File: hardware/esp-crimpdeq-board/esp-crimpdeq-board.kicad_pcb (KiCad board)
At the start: 2 copper layers, 22.9 x 63.5 mm, 95 parts, among them J1 USB4105-GF-A, Q1 DMG3415U, SW1 SW_Push, SW2 SW_Push, U1 SHTC3, U2 ICM-42670-P, U3 ESP32-C3-MINI-1, U4 Rust_Board, U5 SY8088, U6 MCP73831T-2ACI/OT, Y1 32.768Hz

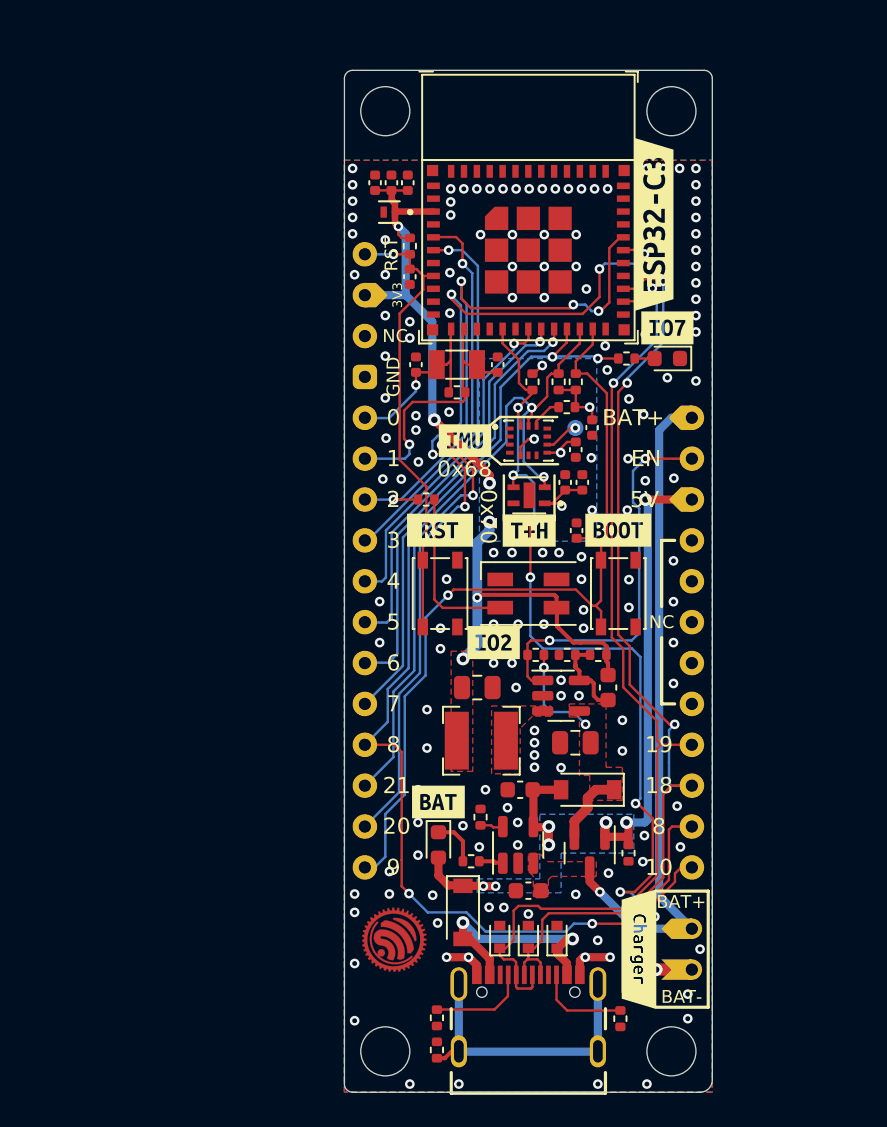
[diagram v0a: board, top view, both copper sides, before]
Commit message: Updated espressif kicad libraries and removed some unecessary libs
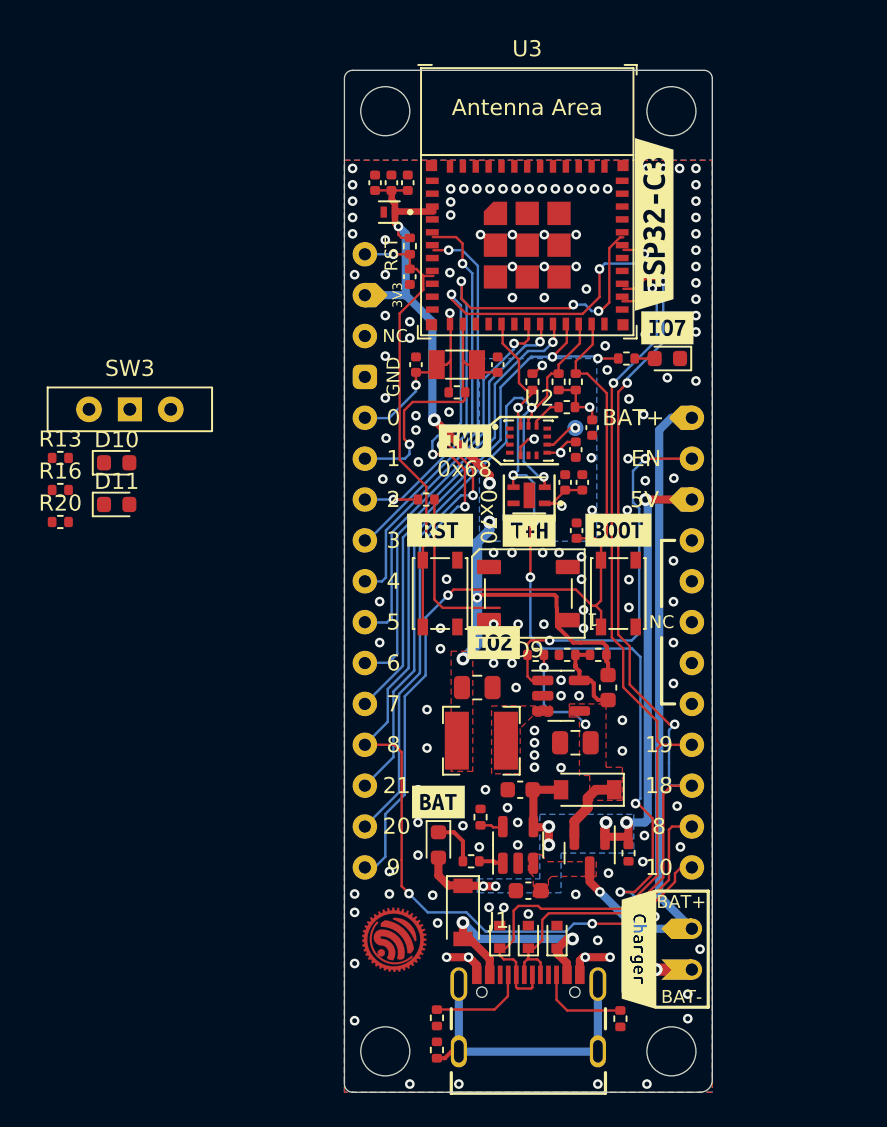
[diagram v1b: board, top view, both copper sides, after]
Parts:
- added D10: LED, LED_SMD:LED_0603_1608Metric, F.Cu at (122.5, 89.4)
- added D11: LED, LED_SMD:LED_0603_1608Metric, F.Cu at (122.5, 92.0)
- added R13: 470R 1%, Resistor_SMD:R_0402_1005Metric, F.Cu at (119.0, 89.1)
- added R16: 470R 1%, Resistor_SMD:R_0402_1005Metric, F.Cu at (119.0, 91.1)
- added R20: 10kR 1%, Resistor_SMD:R_0402_1005Metric, F.Cu at (119.0, 93.1)
- added SW3: SW_Wuerth_450301014042, Button_Switch_THT:SW_Slide-03_Wuerth-WS-SLTV_10x2.5x6.4_P2.54mm, F.Cu at (123.3, 86.1)
- D9: footprint LED_SMD:LED_SK6812MINI_PLCC4_3.5x3.5mm_P1.75mm -> LED_SMD:LED_WS2812B_PLCC4_5.0x5.0mm_P3.2mm
- U3: footprint Espressif:ESP32-C3-MINI-1 -> PCM_Espressif:ESP32-C3-MINI-1
- moved U3 3.01 mm to (148.0, 73.2)
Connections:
- R1 pad 2: ENABLE -> Net-(SW3-A)

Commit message: Changed link libraries
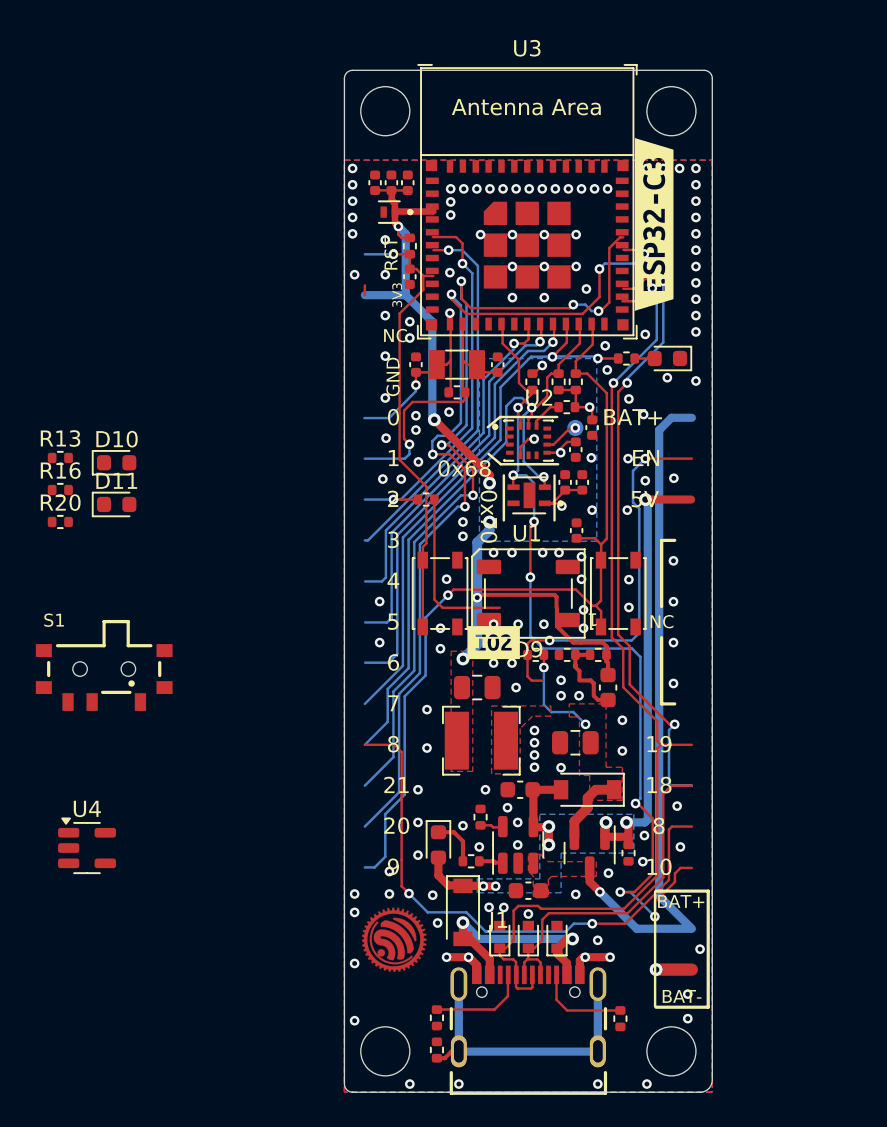
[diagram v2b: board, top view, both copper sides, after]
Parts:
- removed REF**: logo_HF, Rust_Board:logo_HF
- removed REF**: logo_HF, Rust_Board:logo_PB
- removed SW3: SW_Wuerth_450301014042, Button_Switch_THT:SW_Slide-03_Wuerth-WS-SLTV_10x2.5x6.4_P2.54mm
- removed U5: SY8088, Package_TO_SOT_SMD:SOT-23-5
- removed kibuzzard-61B9CCBB, kibuzzard-61B9CE3D, kibuzzard-61B9CE86, kibuzzard-61B9CEAB, kibuzzard-61B9EF98, kibuzzard-61C05335, kibuzzard-61C057D5, kibuzzard-61C057FD, kibuzzard-61C05804, kibuzzard-61C0588C, kibuzzard-61C05909, kibuzzard-61C05949, kibuzzard-61C05975, kibuzzard-61C0597E, kibuzzard-61C05A1A, kibuzzard-61C05A22, kibuzzard-61C05B60, kibuzzard-61C05BAC, kibuzzard-61C05C0D, kibuzzard-61C05C87, kibuzzard-61C05C92, kibuzzard-61C05D58, kibuzzard-61C05D75, kibuzzard-61C05DB0, kibuzzard-61C0F315, kibuzzard-61C0F325, kibuzzard-61C0F363, kibuzzard-61C0F3FF, kibuzzard-61C0F406, kibuzzard-61C0F511, kibuzzard-61C0F551: G***, label
- added S1: 450404015514, PCM_Wurth_Elektronik:450404015514, F.Cu at (121.7, 102.2)
- J1: footprint Rust_Board:GCT_USB4105-GF-A -> PCM_GCT:GCT_USB4105-GF-A
- U1: footprint Rust_Board:SON100P200X200X80-5N -> PCM_Sensirion:SON100P200X200X80-5N
- U2: footprint Rust_Board:IC_ICM-42670-P -> PCM_TDK_InvenSense:IC_ICM-42670-P
- U4: value Rust_Board -> SY8088; footprint Rust_Board:Rust_Board -> Package_TO_SOT_SMD:SOT-23-5
- moved U4 32.4 mm to (120.7, 113.3)
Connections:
- C6 pad 2: Net-(U5-FB) -> Net-(U4-FB)
- R2 pad 2: Net-(U5-FB) -> Net-(U4-FB)
- R3 pad 1: Net-(U5-FB) -> Net-(U4-FB)
- U4 pad 1: CHIP_PU -> ENABLE
- U4 pad 2: +3V3 -> GND
- U4 pad 3: unconnected-(U4-Pad3) -> /Buck_Coil
- U4 pad 4: GND -> +5V
- U4 pad 5: IO0 -> Net-(U4-FB)
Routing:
- net IO21_TX: track 52.2 -> 0.00 mm, vias 5 -> 0
- net IO20_RX: track 55.3 -> 107.5 mm, vias 5 -> 10
- net Net-(R1-Pad2): track 0.00 -> 24.5 mm, vias 0 -> 2
- net ENABLE: track 24.5 -> 0.00 mm, vias 2 -> 0
- net Net-(U5-FB): track 5.25 -> 0.00 mm
- net Net-(U4-FB): track 0.00 -> 5.25 mm

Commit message: Added notes
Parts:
- removed G***: LOGO, Rust_Board:esp-rs_logo_4mm
- removed kibuzzard-61E1AB2E: G***, kibuzzard-61E1AB2E
- removed kibuzzard-61F26841: G***, kibuzzard-61F26841
- removed kibuzzard-61F26855: G***, kibuzzard-61F26855
- removed kibuzzard-61F2685B: G***, kibuzzard-61F2685B
- removed kibuzzard-6269032F: G***, kibuzzard-6269032F
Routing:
- net VBUS: track 39.3 -> 36.5 mm
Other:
- outline, holes or cut-outs redrawn
- board text removed: "-"
- board text removed: "0"
- board text removed: "1"
- board text removed: "1.6mm"
- board text removed: "10"
- board text removed: "18"
- board text removed: "19"
- board text removed: "2"
- board text removed: "20"
- board text removed: "2022-04-27"
- board text removed: "21"
- board text removed: "3"
- board text removed: "4"
- board text removed: "5"
- board text removed: "5V"
- board text removed: "6"
- board text removed: "7"
- board text removed: "8"
- board text removed: "9"
- board text removed: "BAT+"
- board text removed: "BAT-"
- board text removed: "Base Copper (oz)"
- board text removed: "Copper 1 OZ"
- board text removed: "Core"
- board text removed: "DK"
- board text removed: "Date"
- board text removed: "EN"
- board text removed: "ESP-RS"
- board text removed: "ESP32-C3-DevKit-RUST-1"
- board text removed: "ESP32-C3-DevKit-RUST-1 v1.2a 04/2022"
- board text removed: "ESPRESSIF SYSTEMS"
- board text removed: "FR-4 Standard"
- board text removed: "GND"
- board text removed: "Gap"
- board text removed: "I2C Sensors IMU 0x68 T+H 0x70 SDA GPIO10 SCL GPIO8"
- board text removed: "Impedance"
- board text removed: "L1_Top"
- board text removed: "L2_Bottom"
- board text removed: "Material"
- board text removed: "NC"
- board text removed: "RST"
- board text removed: "Rev 1.2a"
- board text removed: "Stackup"
- board text removed: "Task"
- board text removed: "Thickness"
- board text removed: "Thickness (mil)"
- board text removed: "Title"
- board text removed: "Width"
- board text removed: "github.com/esp-rs"

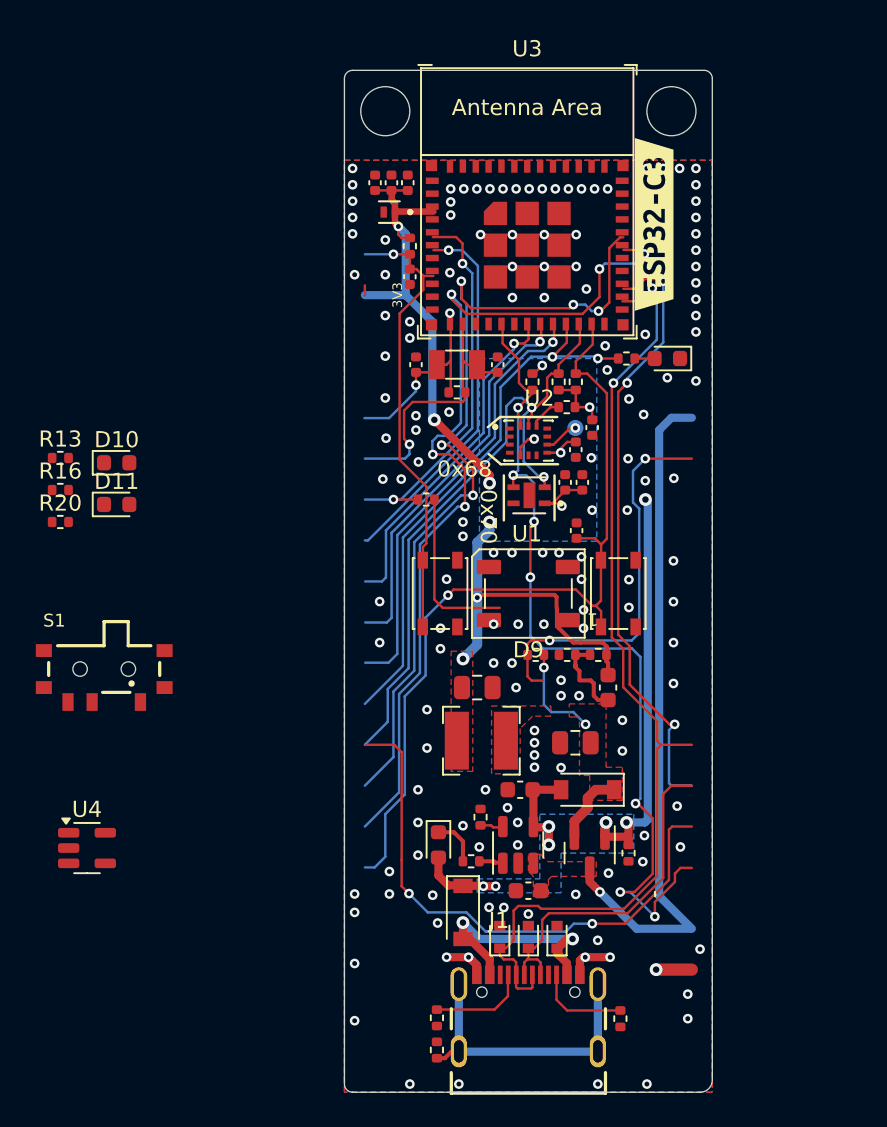
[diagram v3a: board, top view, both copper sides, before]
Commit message: ADC updated
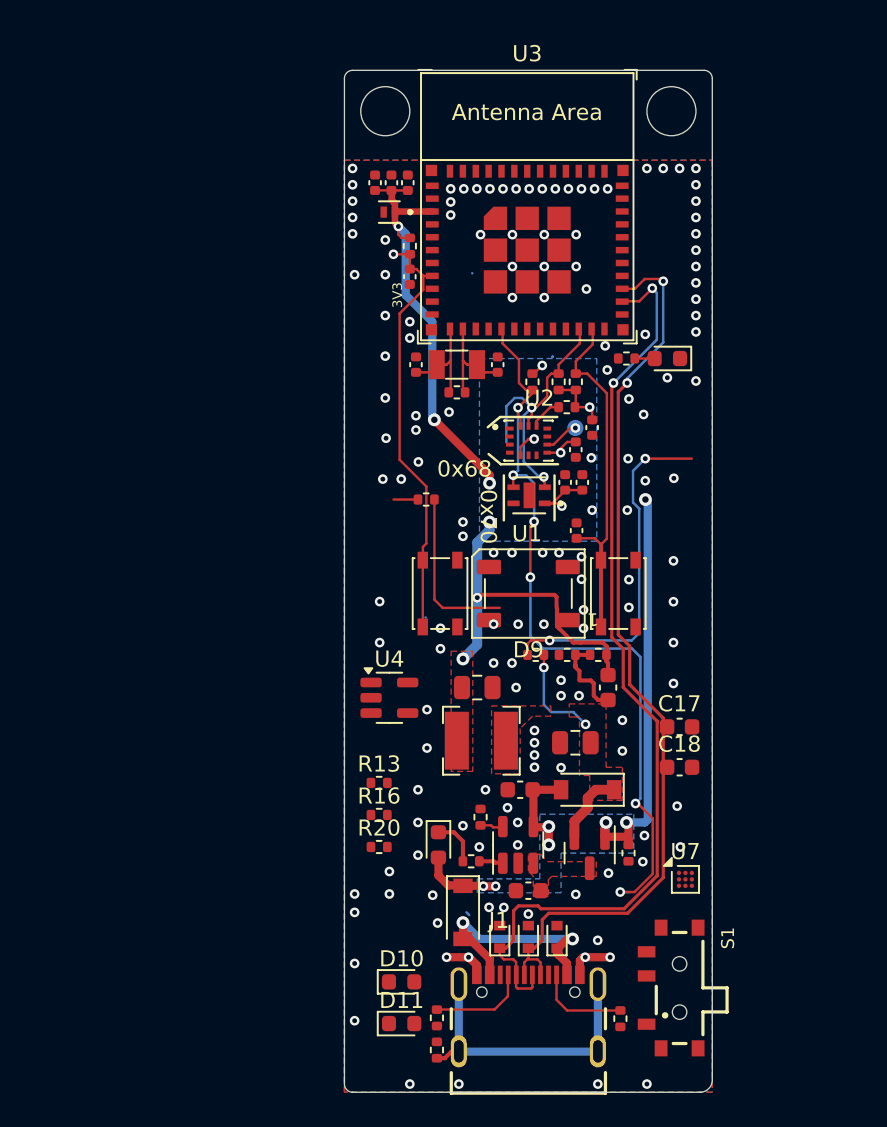
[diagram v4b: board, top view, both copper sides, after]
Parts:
- removed kibuzzard-623DAB98: G***, kibuzzard-623DAB98
- added C17: 0.47uF 16V, Capacitor_SMD:C_0603_1608Metric, F.Cu at (157.5, 105.8)
- added C18: 0.1uF 16V, Capacitor_SMD:C_0603_1608Metric, F.Cu at (157.5, 108.3)
- added U7: ~, Package_BGA:WLP-9_1.468x1.448mm_Layout3x3_P0.4mm, F.Cu at (157.8, 115.3)
- moved S1 40.9 mm to (157.5, 122.0), turned to -90 degrees
- moved D10 36.8 mm to (140.2, 121.7)
- moved D11 36.8 mm to (140.2, 124.3)
- moved R13 28.3 mm to (138.8, 109.3)
- moved R16 28.3 mm to (138.8, 111.3)
- moved R20 28.3 mm to (138.8, 113.3)
- moved U4 21.0 mm to (139.4, 104.0)
- moved U3 0.31 mm to (148.0, 73.5)
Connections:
- net +BATT renamed +BATT_SYS
- R14 pad 1: Net-(U6-STAT) -> IO3
- R20 pad 1: Net-(U6-STAT) -> IO3
- U6 pad 1: Net-(U6-STAT) -> IO3
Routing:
- net IO20_RX: track 107.5 -> 0.00 mm, vias 10 -> 0
- net IO8_SCL: track 74.8 -> 18.1 mm, vias 4 -> 2
- net +BATT_SYS: track 42.4 -> 0.00 mm, vias 1 -> 0
- net IO7: track 33.5 -> 0.05 mm, vias 2 -> 0
- net IO9_BOOT: track 51.5 -> 22.0 mm, vias 1 -> 0
- net IO6: track 27.0 -> 0.00 mm, vias 1 -> 0
- net IO5: track 23.9 -> 0.00 mm, vias 1 -> 0
- net IO2: track 23.8 -> 1.53 mm, vias 2 -> 0
- net IO3: track 23.3 -> 1.50 mm, vias 1 -> 0
- net IO4: track 20.9 -> 0.00 mm, vias 1 -> 0
- net IO1: track 16.8 -> 6.53 mm, vias 1 -> 0
- net IO10_SDA: track 54.8 -> 48.2 mm, vias 7 -> 6
- net IO0: track 11.6 -> 6.52 mm, vias 1 -> 0
- net USB_D+: track 59.9 -> 56.5 mm, vias 3 -> 2
- net +3V3: track 63.0 -> 59.9 mm
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- added copper zone on F.Cu, net +BATT
- removed copper zone on F.Cu, net +BATT_SYS

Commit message: Changed micro
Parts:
- removed D10, D11, D2: LED, LED_SMD:LED_0603_1608Metric
- removed R10, R13, R16: 470R 1%, Resistor_SMD:R_0402_1005Metric
- added U5: NAU7802SGI, Package_SO:SOP-16_3.9x9.9mm_P1.27mm, F.Cu at (164.9, 93.5)
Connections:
- R14 pad 1: IO3 -> IO5
- R17 pad 2: IO8_SCL -> IO4_SCL
- R18 pad 2: IO10_SDA -> IO3_SDA
- R20 pad 1: IO3 -> IO5
- U1 pad 2: IO8_SCL -> IO4_SCL
- U1 pad 3: IO10_SDA -> IO3_SDA
- U2 pad 13: IO8_SCL -> IO4_SCL
- U2 pad 14: IO10_SDA -> IO3_SDA
- U3 pad 16: IO10_SDA -> IO10_SPI2_CS0
- U3 pad 18: IO4 -> IO4_SCL
- U3 pad 19: IO5 -> IO5_CHARGING
- U3 pad 20: IO6 -> IO6_SPI2_CLK
- U3 pad 21: IO7 -> IO7_SPI2_D
- U3 pad 22: IO8_SCL -> IO8_DRDY
- U3 pad 5: IO2 -> IO2_SPI2_Q
- U3 pad 6: IO3 -> IO3_SDA
- U6 pad 1: IO3 -> IO5
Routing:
- net IO5: track 0.00 -> 1.50 mm
- net IO3: track 1.50 -> 0.00 mm
- net (no net): track 0.00 -> 1.32 mm
- net Net-(D2-A): track 1.27 -> 0.00 mm

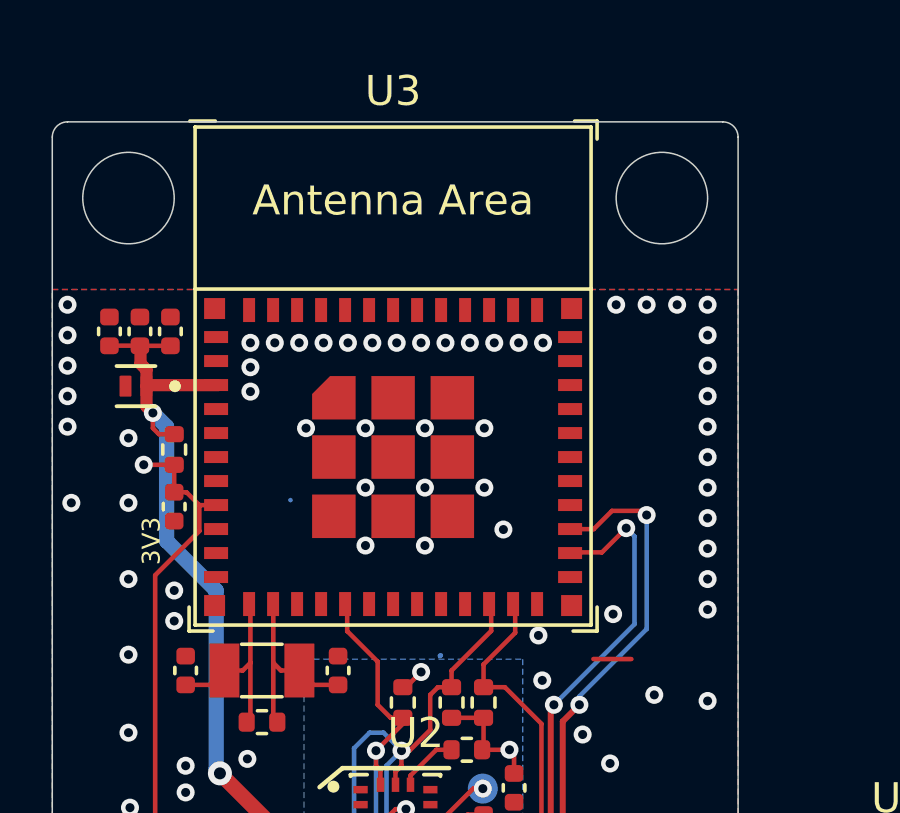
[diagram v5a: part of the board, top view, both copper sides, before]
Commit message: Cahnged uC
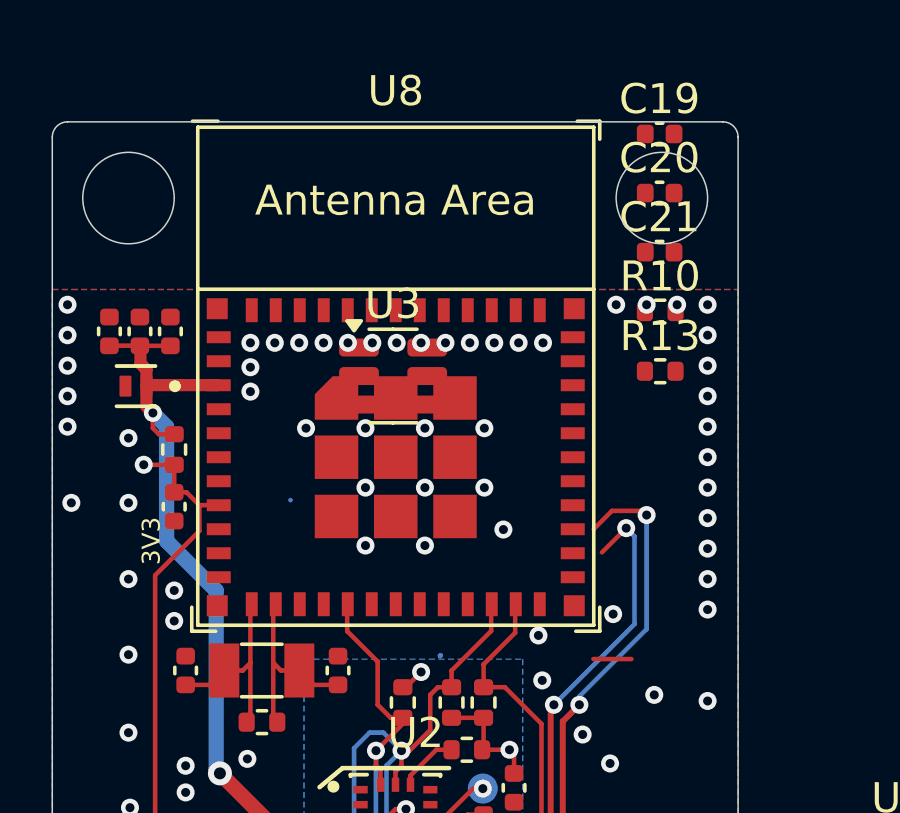
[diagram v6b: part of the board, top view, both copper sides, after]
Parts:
- added C19: 680pF 10V, Capacitor_SMD:C_0402_1005Metric, F.Cu at (156.9, 65.4)
- added C20: 0.1uF 10V, Capacitor_SMD:C_0402_1005Metric, F.Cu at (156.9, 67.4)
- added C21: 0.1uF 10V, Capacitor_SMD:C_0402_1005Metric, F.Cu at (156.9, 69.4)
- added R10: 47R 0.1%, Resistor_SMD:R_0402_1005Metric, F.Cu at (156.9, 71.3)
- added R13: 47R 0.1%, Resistor_SMD:R_0402_1005Metric, F.Cu at (156.9, 73.3)
- added U8: ESP32-C6-MINI-1/U, PCM_Espressif:ESP32-C6-MINI-1, F.Cu at (148.1, 73.5)
- U3: value ESP32-C3-MINI-1 -> REF35330QDBVR; footprint PCM_Espressif:ESP32-C3-MINI-1 -> Package_TO_SOT_SMD:SOT-23-6
- U7: value ~ -> MAX17262
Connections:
- U3 pad 1: GND -> Net-(U3-GND-Pad1)
- U3 pad 2: GND -> Net-(U3-GND-Pad1)
- U3 pad 3: +3V3 -> unconnected-(U3-EN-Pad3)
- U3 pad 5: IO2_SPI2_Q -> unconnected-(U3-NR-Pad5)
- U3 pad 6: IO3_SDA -> unconnected-(U3-VREF-Pad6)
- U5 pad 2: unconnected-(U5-VIN1N-Pad2) -> Net-(U5-VIN1N)
- U5 pad 3: unconnected-(U5-VIN1P-Pad3) -> Net-(U5-VIN1P)
- U5 pad 4: unconnected-(U5-VIN2N-Pad4) -> Net-(U5-VIN2N)
- U5 pad 5: unconnected-(U5-VIN2P-Pad5) -> Net-(U5-VIN2P)
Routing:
- net IO3_SDA: track 0.00 -> 48.2 mm, vias 0 -> 6
- net IO10_SDA: track 48.2 -> 0.00 mm, vias 6 -> 0
- net IO8_SCL: track 18.1 -> 0.24 mm, vias 2 -> 0
- net IO4_SCL: track 0.00 -> 17.9 mm, vias 0 -> 2
- net USB_D-: track 59.2 -> 58.1 mm
- net USB_D+: track 56.5 -> 55.8 mm

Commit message: + work
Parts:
- added R21: 10kR 1%, Resistor_SMD:R_0402_1005Metric, F.Cu at (162.1, 81.6)
- added R22: 10kR 1%, Resistor_SMD:R_0402_1005Metric, F.Cu at (162.1, 83.6)
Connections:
- U1 pad 2: IO4_SCL -> IOX_LP_SCL
- U1 pad 3: IO3_SDA -> IOX_LP_SDA
- U3 pad 6: unconnected-(U3-VREF-Pad6) -> Net-(U3-VREF)
- U5 pad 1: unconnected-(U5-REFP-Pad1) -> Net-(U3-VREF)
- U5 pad 13: unconnected-(U5-SCLK-Pad13) -> IO4_SCL
- U5 pad 14: unconnected-(U5-SDIO-Pad14) -> IO3_SDA
- U7 pad B1: IO8_SCL -> IOX_LP_SCL
- U7 pad C1: IO10_SDA -> IOX_LP_SDA
